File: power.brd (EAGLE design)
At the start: 92.1 x 79.4 mm, 61 parts, among them IC1 7812DT, IC2 7805TV, IC3 78L05F, U1 P82B96D, U2 P82B96D

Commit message: ****ing pinouts
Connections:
- removed net N$51: OK3.P$3, U1.7
- new net N$6: OK3.P$3, U1.5
- net N$30: now also U1.7; no longer U1.5
- net N$50: now also U1.3; no longer U1.1
- net N$54: now also U2.3; no longer U2.1
- net N$55: now also U2.5; no longer U2.7
- net N$8: now also U1.1; no longer U1.3
- net SCL: now also U2.7; no longer U2.5
- net SDA: now also U2.1; no longer U2.3
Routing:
- net N$51: track 21.2 -> 0.00 mm
- net N$6: track 0.00 -> 20.0 mm
- net N$54: track 10.4 -> 2.10 mm
- net SCL: track 55.0 -> 50.4 mm
- net SDA: track 39.1 -> 35.9 mm
- net N$55: track 24.3 -> 22.4 mm
- net N$30: track 28.1 -> 26.1 mm
- net N$8: track 33.3 -> 31.3 mm
- net N$50: track 32.6 -> 31.4 mm
- net N$15: track 56.2 -> 57.2 mm
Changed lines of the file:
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@@
 <contactref element="D1" pad="A"/>
 <wire x1="15.875" y1="41.91" x2="15.875" y2="43.815" width="0.8128" layer="16"/>
-<wire x1="15.875" y1="43.815" x2="19.685" y2="47.625" width="0.8128" layer="16"/>
-<wire x1="19.685" y1="47.625" x2="68.58" y2="47.625" width="0.8128" layer="16"/>
+<wire x1="15.875" y1="43.815" x2="20.955" y2="48.895" width="0.8128" layer="16"/>
+<wire x1="20.955" y1="48.895" x2="43.815" y2="48.895" width="0.8128" layer="16"/>
+<wire x1="43.815" y1="48.895" x2="45.085" y2="47.625" width="0.8128" layer="16"/>
+<wire x1="45.085" y1="47.625" x2="68.58" y2="47.625" width="0.8128" layer="16"/>
 </signal>
 <signal name="AIN0">
@@
 <wire x1="49.53" y1="14.605" x2="48.26" y2="13.335" width="0.254" layer="16"/>
 <wire x1="48.26" y1="13.335" x2="48.26" y2="8.47" width="0.254" layer="16"/>
-<contactref element="U2" pad="3"/>
 <wire x1="49.53" y1="14.605" x2="52.705" y2="17.78" width="0.254" layer="16"/>
 <wire x1="52.705" y1="17.78" x2="52.705" y2="18.415" width="0.254" layer="16"/>
 <wire x1="52.705" y1="18.415" x2="53.34" y2="19.05" width="0.254" layer="16"/>
-<wire x1="53.34" y1="19.05" x2="55.1688" y2="19.05" width="0.254" layer="16"/>
-<wire x1="55.1688" y1="19.05" x2="56.515" y2="19.05" width="0.254" layer="16"/>
 <wire x1="56.515" y1="19.05" x2="58.42" y2="17.145" width="0.254" layer="16"/>
 <wire x1="58.42" y1="17.145" x2="74.295" y2="17.145" width="0.254" layer="16"/>
 <wire x1="74.295" y1="17.145" x2="76.7" y2="14.74" width="0.254" layer="16"/>
 <wire x1="76.7" y1="14.74" x2="77.96" y2="14.74" width="0.254" layer="16"/>
+<contactref element="U2" pad="1"/>
+<wire x1="55.1688" y1="21.59" x2="56.515" y2="19.05" width="0" layer="19" extent="16-16"/>
+<wire x1="53.34" y1="19.05" x2="55.1688" y2="21.59" width="0" layer="19" extent="16-16"/>
 </signal>
 <signal name="SCL">
@@
 <wire x1="46.99" y1="14.605" x2="45.72" y2="13.335" width="0.254" layer="16"/>
 <wire x1="45.72" y1="13.335" x2="45.72" y2="8.47" width="0.254" layer="16"/>
-<contactref element="U2" pad="5"/>
 <wire x1="46.99" y1="14.605" x2="46.99" y2="15.875" width="0.254" layer="16"/>
 <wire x1="46.99" y1="15.875" x2="48.895" y2="17.78" width="0.254" layer="16"/>
-<wire x1="48.895" y1="17.78" x2="50.2412" y2="17.78" width="0.254" layer="16"/>
-<wire x1="50.2412" y1="17.78" x2="46.99" y2="17.78" width="0.254" layer="16"/>
 <via x="46.99" y="17.78" extent="1-16" drill="0.6" shape="square"/>
 <wire x1="46.99" y1="17.78" x2="74.295" y2="17.78" width="0.254" layer="1"/>
@@
 <wire x1="77.96" y1="14.24" x2="78.105" y2="14.095" width="0.254" layer="16"/>
 <wire x1="78.105" y1="14.095" x2="78.105" y2="13.335" width="0.254" layer="16"/>
+<contactref element="U2" pad="7"/>
+<wire x1="48.895" y1="17.78" x2="50.2412" y2="20.32" width="0" layer="19" extent="16-16"/>
+<wire x1="46.99" y1="17.78" x2="46.99" y2="15.875" width="0" layer="19" extent="16-16"/>
 </signal>
 <signal name="+3V3">
@@
 </signal>
 <signal name="N$8">
-<contactref element="U1" pad="3"/>
 <wire x1="10.795" y1="48.895" x2="15.24" y2="44.45" width="0.254" layer="1"/>
 <wire x1="15.24" y1="44.45" x2="28.575" y2="44.45" width="0.254" layer="1"/>
@@
 <wire x1="31.75" y1="41.275" x2="34.925" y2="41.275" width="0.254" layer="1"/>
 <via x="34.925" y="41.275" extent="1-16" drill="0.6" shape="square"/>
-<wire x1="34.925" y1="41.275" x2="32.9438" y2="41.275" width="0.254" layer="16"/>
 <contactref element="U$1" pad="7"/>
 <wire x1="10.795" y1="48.895" x2="10.795" y2="51.435" width="0.254" layer="1"/>
@@
 <wire x1="10.795" y1="51.435" x2="10.66" y2="51.57" width="0.254" layer="16"/>
 <wire x1="10.66" y1="51.57" x2="9.38" y2="51.57" width="0.254" layer="16"/>
+<contactref element="U1" pad="1"/>
+<wire x1="31.75" y1="41.275" x2="32.9438" y2="43.815" width="0" layer="19" extent="1-16"/>
 </signal>
 <signal name="N$30">
-<contactref element="U1" pad="5"/>
 <wire x1="8.255" y1="50.165" x2="8.255" y2="45.72" width="0.254" layer="1"/>
 <wire x1="8.255" y1="45.72" x2="13.97" y2="40.005" width="0.254" layer="1"/>
 <wire x1="13.97" y1="40.005" x2="26.035" y2="40.005" width="0.254" layer="1"/>
 <via x="26.035" y="40.005" extent="1-16" drill="0.6" shape="square"/>
-<wire x1="26.035" y1="40.005" x2="28.0162" y2="40.005" width="0.254" layer="16"/>
 <contactref element="U$1" pad="6"/>
 <via x="8.255" y="50.165" extent="1-16" drill="0.6" shape="square"/>
 <wire x1="8.255" y1="50.165" x2="9.16" y2="51.07" width="0.254" layer="16"/>
 <wire x1="9.16" y1="51.07" x2="9.38" y2="51.07" width="0.254" layer="16"/>
+<contactref element="U1" pad="7"/>
+<wire x1="26.035" y1="40.005" x2="28.0162" y2="42.545" width="0" layer="19" extent="16-16"/>
 </signal>
 <signal name="N$14">
@@
 </signal>
 <signal name="N$50">
-<contactref element="U1" pad="1"/>
 <contactref element="OK1" pad="P$3"/>
-<wire x1="32.9438" y1="43.815" x2="31.75" y2="43.815" width="0.254" layer="16"/>
 <wire x1="31.75" y1="43.815" x2="31.115" y2="43.18" width="0.254" layer="16"/>
 <wire x1="31.115" y1="43.18" x2="31.115" y2="39.37" width="0.254" layer="16"/>
@@
 <wire x1="33.02" y1="37.465" x2="50.8635" y2="37.465" width="0.254" layer="16"/>
 <wire x1="50.8635" y1="37.465" x2="55.245" y2="33.0835" width="0.254" layer="16"/>
-</signal>
-<signal name="N$51">
-<contactref element="U1" pad="7"/>
-<contactref element="OK3" pad="P$3"/>
-<wire x1="28.0162" y1="42.545" x2="29.21" y2="42.545" width="0.254" layer="16"/>
-<wire x1="29.21" y1="42.545" x2="30.48" y2="41.275" width="0.254" layer="16"/>
-<wire x1="30.48" y1="41.275" x2="30.48" y2="38.735" width="0.254" layer="16"/>
-<wire x1="30.48" y1="38.735" x2="32.385" y2="36.83" width="0.254" layer="16"/>
-<wire x1="32.385" y1="36.83" x2="40.0685" y2="36.83" width="0.254" layer="16"/>
-<wire x1="40.0685" y1="36.83" x2="43.815" y2="33.0835" width="0.254" layer="16"/>
+<contactref element="U1" pad="3"/>
+<wire x1="31.115" y1="43.18" x2="32.9438" y2="41.275" width="0" layer="19" extent="16-16"/>
 </signal>
 <signal name="N$53">
@@
 </signal>
 <signal name="N$54">
-<contactref element="U2" pad="1"/>
 <contactref element="OK2" pad="P$3"/>
-<wire x1="55.1688" y1="21.59" x2="63.5" y2="21.59" width="0.254" layer="16"/>
 <wire x1="63.5" y1="21.59" x2="64.135" y2="22.225" width="0.254" layer="16"/>
 <wire x1="64.135" y1="22.225" x2="64.135" y2="23.4315" width="0.254" layer="16"/>
+<contactref element="U2" pad="3"/>
+<wire x1="55.1688" y1="19.05" x2="63.5" y2="21.59" width="0" layer="19" extent="16-16"/>
 </signal>
 <signal name="N$55">
-<contactref element="U2" pad="7"/>
 <contactref element="OK4" pad="P$3"/>
 <wire x1="29.845" y1="25.9715" x2="29.845" y2="24.13" width="0.254" layer="16"/>
@@
 <wire x1="42.545" y1="20.32" x2="48.26" y2="20.32" width="0.254" layer="1"/>
 <via x="48.26" y="20.32" extent="1-16" drill="0.6" shape="square"/>
-<wire x1="48.26" y1="20.32" x2="50.2412" y2="20.32" width="0.254" layer="16"/>
+<contactref element="U2" pad="5"/>
+<wire x1="48.26" y1="20.32" x2="50.2412" y2="17.78" width="0" layer="19" extent="16-16"/>
 </signal>
 <signal name="N$56">
@@
 <wire x1="4.725" y1="16.25" x2="6.985" y2="13.99" width="0.3048" layer="16"/>
 </signal>
+<signal name="N$6">
+<contactref element="U1" pad="5"/>
+<contactref element="OK3" pad="P$3"/>
+<wire x1="29.21" y1="42.545" x2="30.48" y2="41.275" width="0.254" layer="16"/>
+<wire x1="30.48" y1="41.275" x2="30.48" y2="38.735" width="0.254" layer="16"/>
+<wire x1="30.48" y1="38.735" x2="32.385" y2="36.83" width="0.254" layer="16"/>
+<wire x1="32.385" y1="36.83" x2="40.0685" y2="36.83" width="0.254" layer="16"/>
+<wire x1="40.0685" y1="36.83" x2="43.815" y2="33.0835" width="0.254" layer="16"/>
+<wire x1="30.48" y1="41.275" x2="28.0162" y2="40.005" width="0" layer="19" extent="16-16"/>
+</signal>
 </signals>

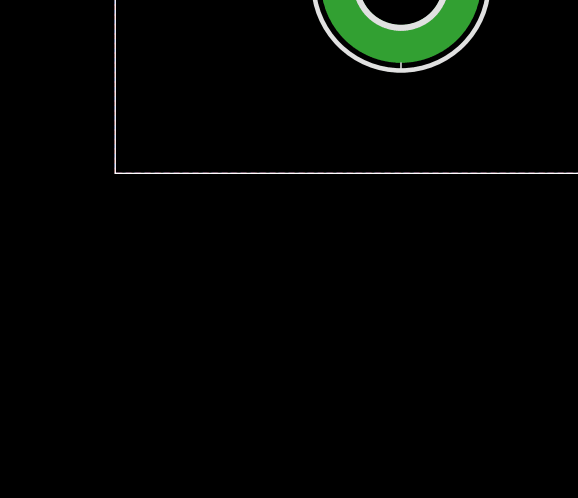
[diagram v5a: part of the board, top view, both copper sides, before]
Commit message: found more mistakes in the isolated i2c bus
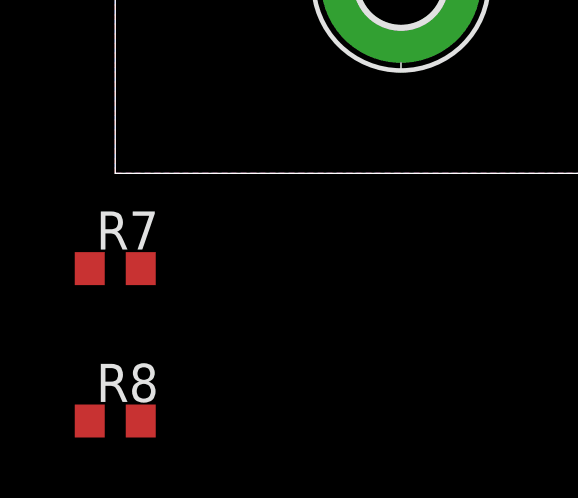
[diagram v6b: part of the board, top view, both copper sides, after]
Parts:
- added R7, R8: 47k, rcl:R0603
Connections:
- net N$14: now also R7.1
- net N$43: now also R7.2, R8.2
- net N$53: now also R8.1
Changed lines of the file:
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@@
 <element name="C5" library="rcl" package="C0603K" value="0.1u" x="38.735" y="20.955" rot="MR270"/>
 <element name="C6" library="rcl" package="E5-10,5" value="100u" x="2.54" y="60.325" rot="R180"/>
+<element name="R7" library="rcl" package="R0603" value="47k" x="-3.175" y="-6.35"/>
+<element name="R8" library="rcl" package="R0603" value="47k" x="-3.175" y="-11.43"/>
 </elements>
 <signals>
@@
 <wire x1="39.37" y1="38.735" x2="57.8485" y2="38.735" width="0.254" layer="16"/>
 <wire x1="57.8485" y1="38.735" x2="64.135" y2="32.4485" width="0.254" layer="16"/>
+<contactref element="R7" pad="1"/>
+<wire x1="-4.025" y1="-6.35" x2="32.9438" y2="42.545" width="0" layer="19" extent="1-16"/>
 </signal>
 <signal name="N$7">
@@
 <wire x1="29.21" y1="41.275" x2="29.845" y2="40.64" width="0.254" layer="16"/>
 <wire x1="29.845" y1="40.64" x2="29.845" y2="34.9885" width="0.254" layer="16"/>
+<contactref element="R8" pad="1"/>
+<wire x1="-4.025" y1="-11.43" x2="29.845" y2="34.9885" width="0" layer="19" extent="1-16"/>
 </signal>
 <signal name="N$54">
@@
 <via x="46.99" y="35.56" extent="1-16" drill="0.6" shape="square"/>
 <wire x1="46.99" y1="35.56" x2="46.99" y2="30.48" width="0.3048" layer="1"/>
+<contactref element="R7" pad="2"/>
+<contactref element="R8" pad="2"/>
+<wire x1="-2.325" y1="-6.35" x2="7.849" y2="19.609" width="0" layer="19" extent="1-16"/>
+<wire x1="-2.325" y1="-11.43" x2="-2.325" y2="-6.35" width="0" layer="19" extent="1-1"/>
 </signal>
 <signal name="N$46">

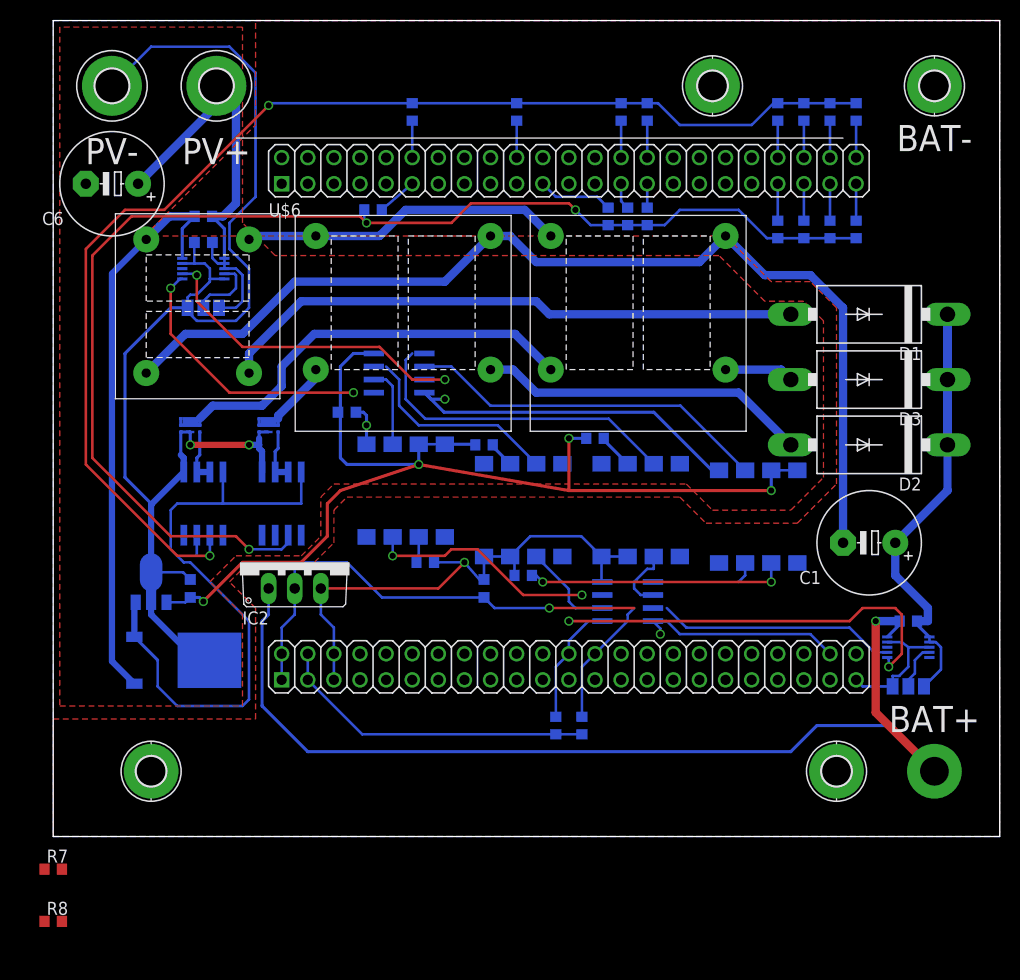
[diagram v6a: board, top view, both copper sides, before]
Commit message: Cluttering up the schematic some more
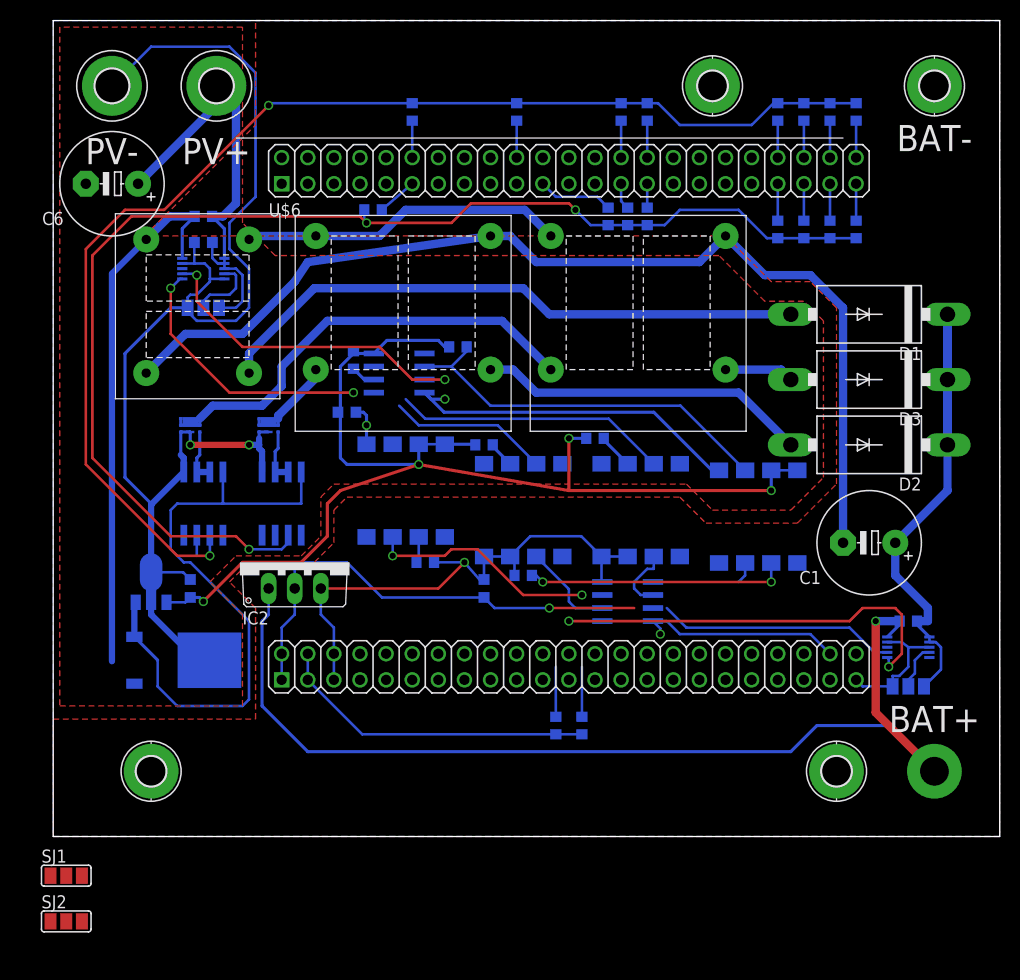
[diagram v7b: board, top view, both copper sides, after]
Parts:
- added SJ1, SJ2: (no value), jumper:SJ_2
- moved R7 64.3 mm to (36.2, 44.5), flipped to the bottom
- moved R8 61.9 mm to (26.0, 43.2), flipped to the bottom, turned to 90 degrees
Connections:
- new net N$17: SJ1.3, U$6.64
- new net N$18: SJ1.1, U$6.66
- new net N$19: SJ2.1, U$6.63
- new net N$20: SJ2.3, U$6.65
- net PGND: now also IC1.1; no longer IC1.3
- net PVIN: now also IC1.3; no longer IC1.1
- net SCL: now also SJ2.2; no longer U$6.70
- net SDA: now also SJ1.2; no longer U$6.72
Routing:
- net N$43: track 105.7 -> 114.1 mm
- net SDA: track 35.9 -> 28.1 mm
- net SCL: track 50.4 -> 44.6 mm
- net N$53: track 7.74 -> 2.42 mm
- net N$50: track 31.4 -> 26.7 mm
- net N$6: track 20.0 -> 15.7 mm
- net PVIN: track 55.7 -> 52.6 mm
- net N$14: track 35.4 -> 37.9 mm
- net PGND: track 166.8 -> 165.6 mm
- net N$3: track 43.3 -> 44.3 mm
- net N$15: track 57.2 -> 58.3 mm
- net GND: track 183.0 -> 182.4 mm

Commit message: Pulled the hard stuff out of the schematic Still needs some work and a board redo
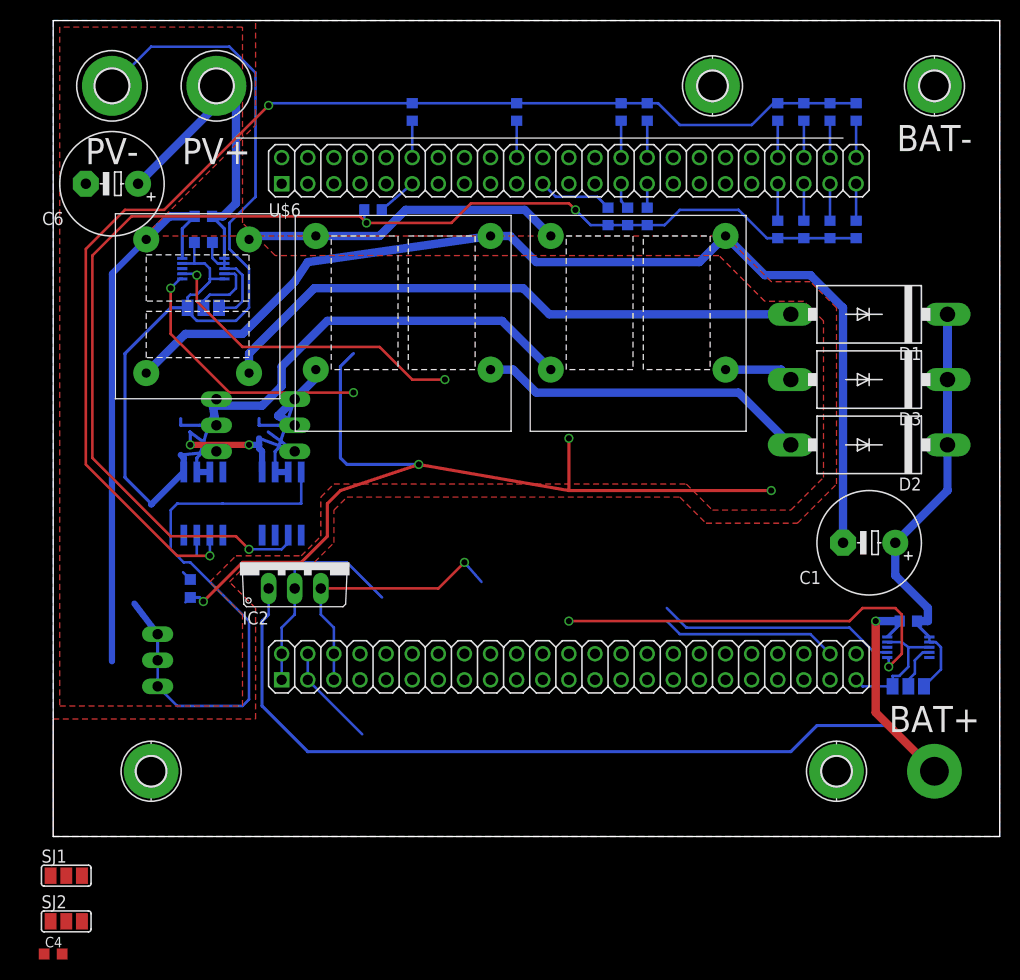
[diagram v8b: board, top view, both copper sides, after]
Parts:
- removed C5: 0.1u, rcl:C0603K
- removed IC3: 78L05F, linear:SOT89
- removed OK1, OK2, OK3, OK4: 6N137SMD, semiconductors:8-SMD
- removed R3, R4, R7, R8: 47k, rcl:R0603
- removed R31, R32, R5, R6: 560, rcl:R0603
- removed U1, U2: P82B96D, semiconductors:SOIC127P600X175-8N
- IC1: value 7812DT -> 7815TV; device linear:TO252 -> linear:TO220V
- U$7, U$8: value SIA446DJ -> IRF740; device semiconductors:SC70-6L -> transistor-power:TO220BV
- moved C4 60.0 mm to (-3.17, -14.6), flipped to the top, turned to 0 degrees
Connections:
- removed net N$14: OK2.P$6, R7.1, U1.2
- removed net N$30: U$1.6, U1.7
- removed net N$39: OK4.P$2, R6.2
- removed net N$43: C2.1, C4.1, IC3.1, OK2.P$7, OK2.P$8, OK4.P$7, OK4.P$8, R31.2, R32.2, R7.2, R8.2, U1.8
- removed net N$48: OK3.P$2, R32.1
- removed net N$49: OK1.P$2, R31.1
- removed net N$50: OK1.P$3, U1.3
- removed net N$53: OK4.P$6, R8.1, U1.6
- removed net N$54: OK2.P$3, U2.3
- removed net N$55: OK4.P$3, U2.5
- removed net N$56: OK1.P$6, U2.2
- removed net N$57: OK3.P$6, U2.6
- removed net N$6: OK3.P$3, U1.5
- removed net N$7: OK2.P$2, R5.2
- removed net N$8: U$1.7, U1.1
- removed net PGND: C2.2, C3.2, C4.2, C6.-, IC1.1, IC3.2, IC3.2@1, OK2.P$5, OK4.P$5, PV-.B3,3, SJ5.1, U$1.5, U$1.9, U$10.5, U$7.4, U$7.7, U$8.4, U$8.7, U$9.5, U1.4
- net +3V3: no longer R3.2, R4.2
- net GND: now also C2.2, C3.2, C4.2, C6.-, IC1.2, PV-.B3,3, SJ5.1, U$1.5, U$1.9, U$10.5, U$7.S, U$8.S, U$9.5; no longer C5.2, U2.4
- net N$13: now also U$8.G; no longer U$8.3
- net N$16: now also U$7.G; no longer U$7.3
- net N$2: now also U$7.D; no longer U$7.1, U$7.2, U$7.5, U$7.6
- net N$3: now also U$8.D; no longer U$8.1, U$8.2, U$8.5, U$8.6
- net N$4: now also C4.1, IC1.1
- net N$46: now also C2.1, IC1.3; no longer IC1.2, IC3.3, U$10.8
- net PVIN: now also U$10.8; no longer IC1.3
- net SCL: now also U$1.6; no longer R4.1, U2.7
- net SDA: now also U$1.7; no longer R3.1, U2.1
- net VCC: no longer C5.1, OK1.P$7, OK1.P$8, OK3.P$7, OK3.P$8, R5.1, R6.1, U2.8
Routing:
- net PGND: track 165.6 -> 0.00 mm, vias 4 -> 0
- net N$43: track 114.1 -> 0.00 mm, vias 4 -> 0
- net GND: track 182.4 -> 270.3 mm
- net N$46: track 60.2 -> 144.7 mm, vias 0 -> 4
- net N$14: track 37.9 -> 0.00 mm
- net N$8: track 31.3 -> 0.00 mm, vias 2 -> 0
- net N$50: track 26.7 -> 0.00 mm
- net SDA: track 28.1 -> 54.5 mm, vias 0 -> 2
- net N$30: track 26.1 -> 0.00 mm, vias 2 -> 0
- net VCC: track 52.6 -> 27.0 mm
- net N$7: track 25.4 -> 0.00 mm, vias 2 -> 0
- net N$55: track 22.4 -> 0.00 mm, vias 2 -> 0
- net +3V3: track 31.4 -> 10.0 mm
- net SCL: track 44.6 -> 65.8 mm, vias 2 -> 4
- net N$6: track 15.7 -> 0.00 mm
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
